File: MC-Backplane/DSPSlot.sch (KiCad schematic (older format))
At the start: 1 part

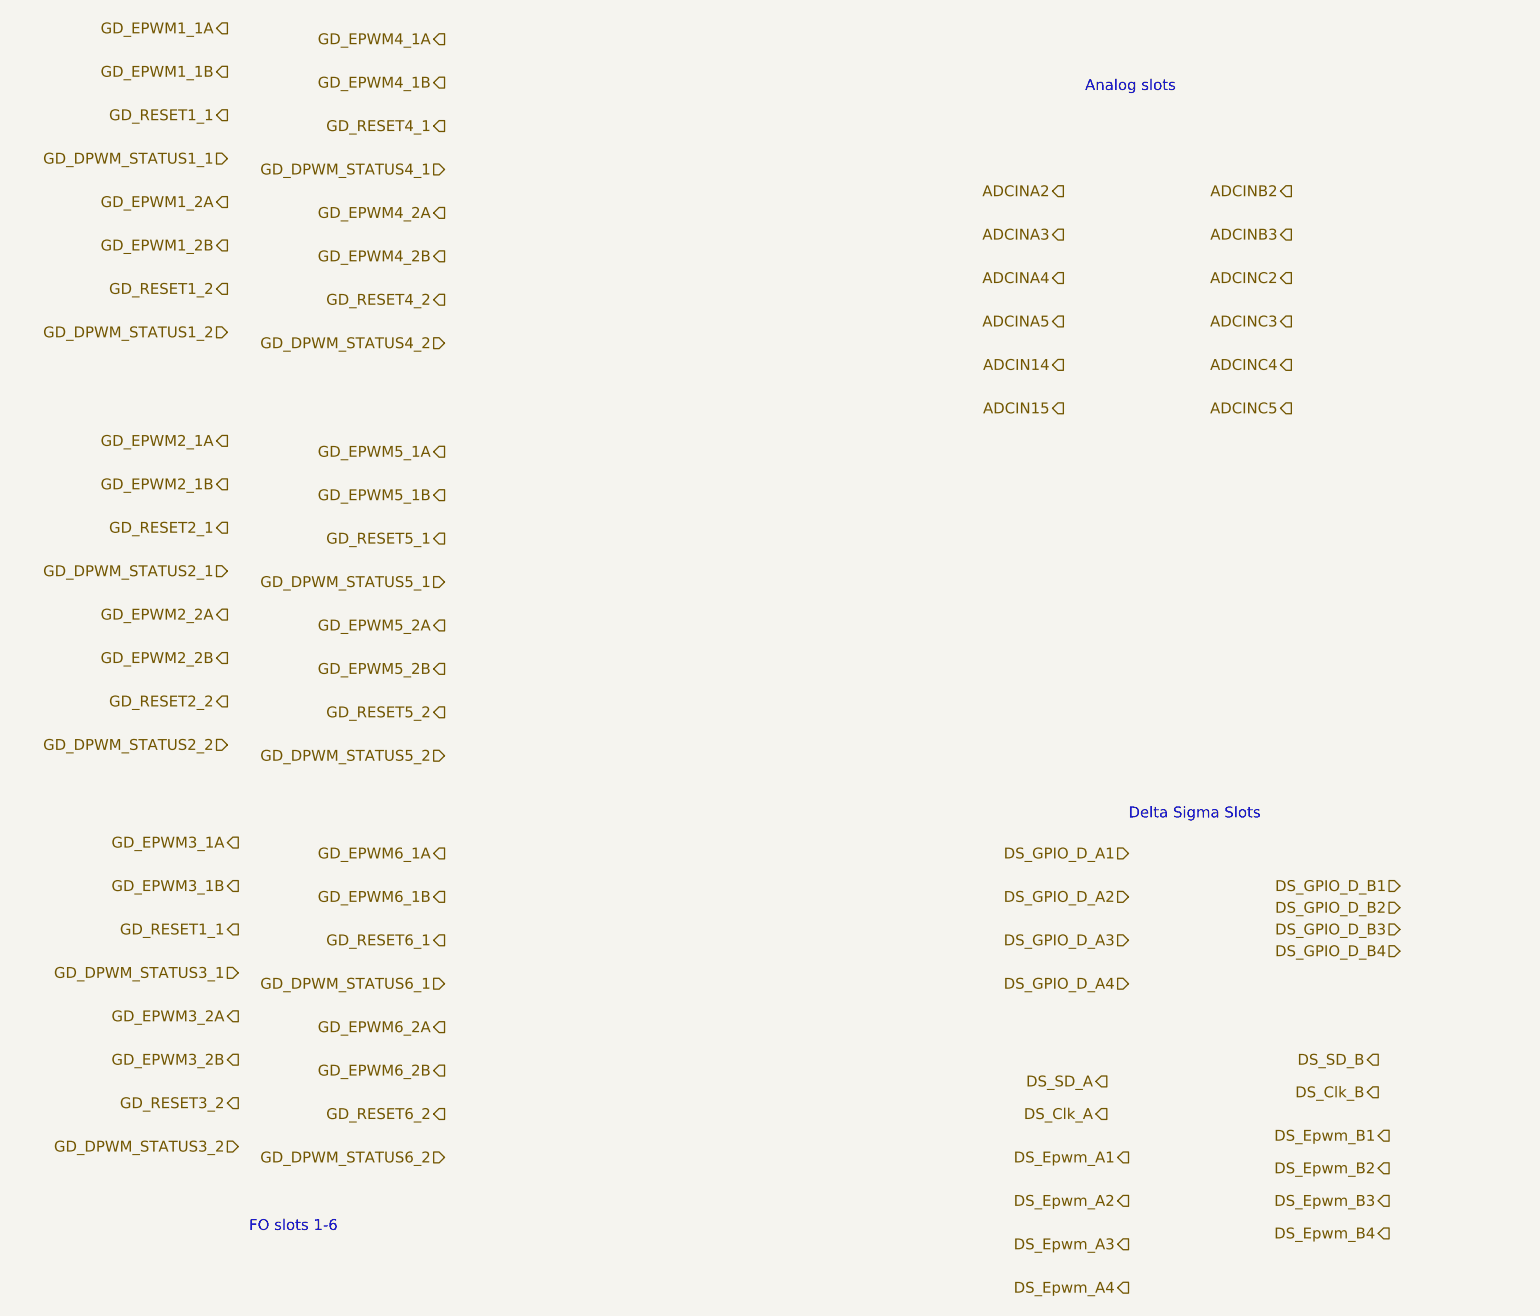
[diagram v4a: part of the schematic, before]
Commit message: Signal naming cleanup/ dsp pin pairing
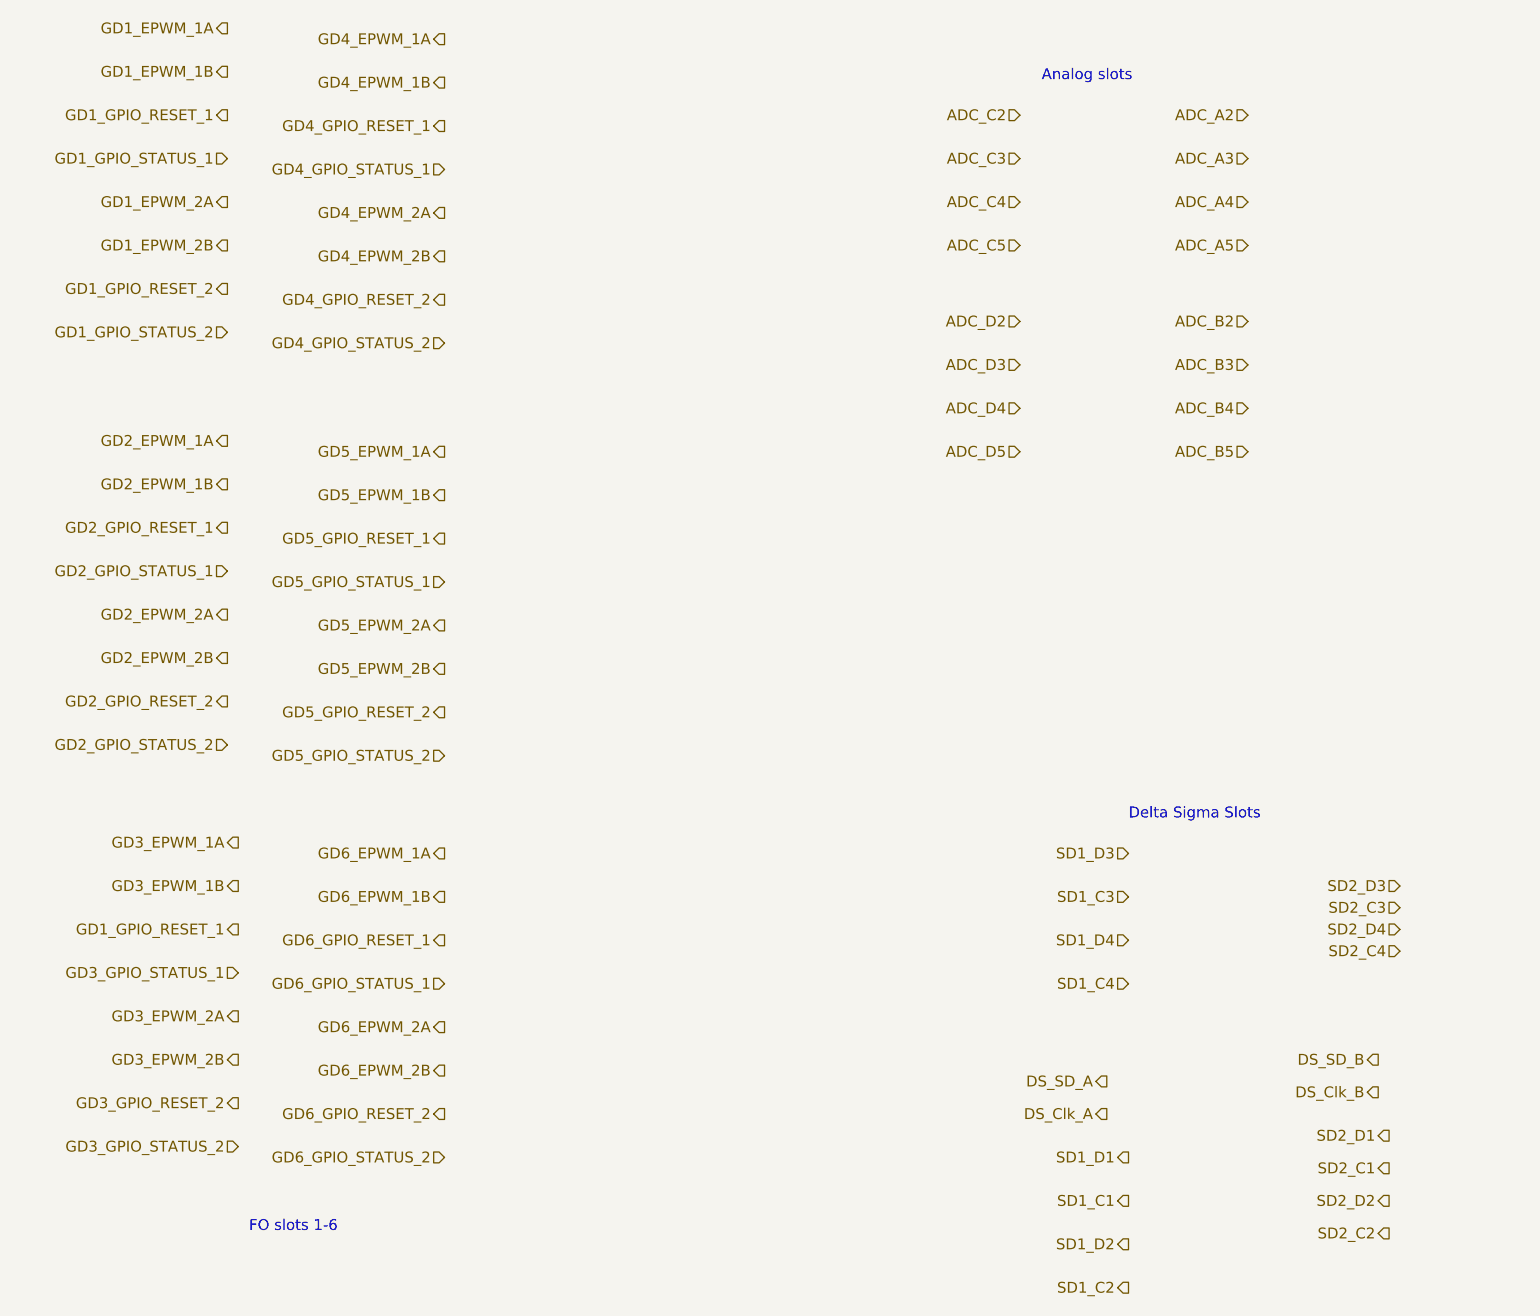
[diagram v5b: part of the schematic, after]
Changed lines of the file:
@@
 placeholder connector
 Text HLabel 1650 750  0    50   Output ~ 0
-GD_EPWM1_1A
+GD1_EPWM_1A
 Text HLabel 1650 950  0    50   Output ~ 0
-GD_EPWM1_1B
+GD1_EPWM_1B
 Text HLabel 1650 1150 0    50   Output ~ 0
-GD_RESET1_1
+GD1_GPIO_RESET_1
 Text HLabel 1650 1350 0    50   Input ~ 0
-GD_DPWM_STATUS1_1
+GD1_GPIO_STATUS_1
 Text HLabel 1650 1550 0    50   Output ~ 0
-GD_EPWM1_2A
+GD1_EPWM_2A
 Text HLabel 1650 1750 0    50   Output ~ 0
-GD_EPWM1_2B
+GD1_EPWM_2B
 Text HLabel 1650 1950 0    50   Output ~ 0
-GD_RESET1_2
+GD1_GPIO_RESET_2
 Text HLabel 1650 2150 0    50   Input ~ 0
-GD_DPWM_STATUS1_2
+GD1_GPIO_STATUS_2
 Text HLabel 1650 2650 0    50   Output ~ 0
-GD_EPWM2_1A
+GD2_EPWM_1A
 Text HLabel 1650 2850 0    50   Output ~ 0
-GD_EPWM2_1B
+GD2_EPWM_1B
 Text HLabel 1650 3050 0    50   Output ~ 0
-GD_RESET2_1
+GD2_GPIO_RESET_1
 Text HLabel 1650 3250 0    50   Input ~ 0
-GD_DPWM_STATUS2_1
+GD2_GPIO_STATUS_1
 Text HLabel 1650 3450 0    50   Output ~ 0
-GD_EPWM2_2A
+GD2_EPWM_2A
 Text HLabel 1650 3650 0    50   Output ~ 0
-GD_EPWM2_2B
+GD2_EPWM_2B
 Text HLabel 1650 3850 0    50   Output ~ 0
-GD_RESET2_2
+GD2_GPIO_RESET_2
 Text HLabel 1650 4050 0    50   Input ~ 0
-GD_DPWM_STATUS2_2
+GD2_GPIO_STATUS_2
 Text HLabel 1700 4500 0    50   Output ~ 0
-GD_EPWM3_1A
+GD3_EPWM_1A
 Text HLabel 1700 4700 0    50   Output ~ 0
-GD_EPWM3_1B
+GD3_EPWM_1B
 Text HLabel 1700 4900 0    50   Output ~ 0
-GD_RESET1_1
+GD1_GPIO_RESET_1
 Text HLabel 1700 5100 0    50   Input ~ 0
-GD_DPWM_STATUS3_1
+GD3_GPIO_STATUS_1
 Text HLabel 1700 5300 0    50   Output ~ 0
-GD_EPWM3_2A
+GD3_EPWM_2A
 Text HLabel 1700 5500 0    50   Output ~ 0
-GD_EPWM3_2B
+GD3_EPWM_2B
 Text HLabel 1700 5700 0    50   Output ~ 0
-GD_RESET3_2
+GD3_GPIO_RESET_2
 Text HLabel 1700 5900 0    50   Input ~ 0
-GD_DPWM_STATUS3_2
+GD3_GPIO_STATUS_2
 Text HLabel 2650 800  0    50   Output ~ 0
-GD_EPWM4_1A
+GD4_EPWM_1A
 Text HLabel 2650 1000 0    50   Output ~ 0
-GD_EPWM4_1B
+GD4_EPWM_1B
 Text HLabel 2650 1200 0    50   Output ~ 0
-GD_RESET4_1
+GD4_GPIO_RESET_1
 Text HLabel 2650 1400 0    50   Input ~ 0
-GD_DPWM_STATUS4_1
+GD4_GPIO_STATUS_1
 Text HLabel 2650 1600 0    50   Output ~ 0
-GD_EPWM4_2A
+GD4_EPWM_2A
 Text HLabel 2650 1800 0    50   Output ~ 0
-GD_EPWM4_2B
+GD4_EPWM_2B
 Text HLabel 2650 2000 0    50   Output ~ 0
-GD_RESET4_2
+GD4_GPIO_RESET_2
 Text HLabel 2650 2200 0    50   Input ~ 0
-GD_DPWM_STATUS4_2
+GD4_GPIO_STATUS_2
 Text HLabel 2650 4100 0    50   Input ~ 0
-GD_DPWM_STATUS5_2
+GD5_GPIO_STATUS_2
 Text HLabel 2650 3900 0    50   Output ~ 0
-GD_RESET5_2
+GD5_GPIO_RESET_2
 Text HLabel 2650 3700 0    50   Output ~ 0
-GD_EPWM5_2B
+GD5_EPWM_2B
 Text HLabel 2650 3500 0    50   Output ~ 0
-GD_EPWM5_2A
+GD5_EPWM_2A
 Text HLabel 2650 3300 0    50   Input ~ 0
-GD_DPWM_STATUS5_1
+GD5_GPIO_STATUS_1
 Text HLabel 2650 3100 0    50   Output ~ 0
-GD_RESET5_1
+GD5_GPIO_RESET_1
 Text HLabel 2650 2900 0    50   Output ~ 0
-GD_EPWM5_1B
+GD5_EPWM_1B
 Text HLabel 2650 2700 0    50   Output ~ 0
-GD_EPWM5_1A
+GD5_EPWM_1A
 Text HLabel 2650 5950 0    50   Input ~ 0
-GD_DPWM_STATUS6_2
+GD6_GPIO_STATUS_2
 Text HLabel 2650 5750 0    50   Output ~ 0
-GD_RESET6_2
+GD6_GPIO_RESET_2
 Text HLabel 2650 5550 0    50   Output ~ 0
-GD_EPWM6_2B
+GD6_EPWM_2B
 Text HLabel 2650 5350 0    50   Output ~ 0
-GD_EPWM6_2A
+GD6_EPWM_2A
 Text HLabel 2650 5150 0    50   Input ~ 0
-GD_DPWM_STATUS6_1
+GD6_GPIO_STATUS_1
 Text HLabel 2650 4950 0    50   Output ~ 0
-GD_RESET6_1
+GD6_GPIO_RESET_1
 Text HLabel 2650 4750 0    50   Output ~ 0
-GD_EPWM6_1B
+GD6_EPWM_1B
 Text HLabel 2650 4550 0    50   Output ~ 0
-GD_EPWM6_1A
+GD6_EPWM_1A
 Text Notes 1750 6300 0    50   ~ 0
 FO slots 1-6
@@
 Text HLabel 8800 1350 0    50   Input ~ 0
 24V
-Text HLabel 5500 1500 0    50   Output ~ 0
-ADCINA2
-Text HLabel 5500 1700 0    50   Output ~ 0
-ADCINA3
-Text HLabel 5500 1900 0    50   Output ~ 0
-ADCINA4
-Text HLabel 5500 2100 0    50   Output ~ 0
-ADCINA5
-Text HLabel 5500 2300 0    50   Output ~ 0
-ADCIN14
-Text HLabel 5500 2500 0    50   Output ~ 0
-ADCIN15
-Text HLabel 6550 1500 0    50   Output ~ 0
-ADCINB2
-Text HLabel 6550 1700 0    50   Output ~ 0
-ADCINB3
-Text HLabel 6550 1900 0    50   Output ~ 0
-ADCINC2
-Text HLabel 6550 2100 0    50   Output ~ 0
-ADCINC3
-Text HLabel 6550 2300 0    50   Output ~ 0
-ADCINC4
-Text HLabel 6550 2500 0    50   Output ~ 0
-ADCINC5
 Text HLabel 5800 5950 0    50   Output ~ 0
-DS_Epwm_A1
+SD1_D1
 Text HLabel 5800 6150 0    50   Output ~ 0
-DS_Epwm_A2
+SD1_C1
 Text HLabel 5800 6350 0    50   Output ~ 0
-DS_Epwm_A3
+SD1_D2
 Text HLabel 5800 6550 0    50   Output ~ 0
-DS_Epwm_A4
+SD1_C2
 Text HLabel 5700 5600 0    50   Output ~ 0
 DS_SD_A
@@
 DS_Clk_A
 Text HLabel 5800 4550 0    50   Input ~ 0
-DS_GPIO_D_A1
+SD1_D3
 Text HLabel 5800 4750 0    50   Input ~ 0
-DS_GPIO_D_A2
+SD1_C3
 Text HLabel 5800 4950 0    50   Input ~ 0
-DS_GPIO_D_A3
+SD1_D4
 Text HLabel 5800 5150 0    50   Input ~ 0
-DS_GPIO_D_A4
+SD1_C4
 Text HLabel 7000 5850 0    50   Output ~ 0
-DS_Epwm_B1
+SD2_D1
 Text HLabel 7000 6000 0    50   Output ~ 0
-DS_Epwm_B2
+SD2_C1
 Text HLabel 7000 6150 0    50   Output ~ 0
-DS_Epwm_B3
+SD2_D2
 Text HLabel 7000 6300 0    50   Output ~ 0
-DS_Epwm_B4
+SD2_C2
 Text HLabel 6950 5500 0    50   Output ~ 0
 DS_SD_B
@@
 DS_Clk_B
 Text HLabel 7050 4700 0    50   Input ~ 0
-DS_GPIO_D_B1
+SD2_D3
 Text HLabel 7050 4800 0    50   Input ~ 0
-DS_GPIO_D_B2
+SD2_C3
 Text HLabel 7050 4900 0    50   Input ~ 0
-DS_GPIO_D_B3
+SD2_D4
 Text HLabel 7050 5000 0    50   Input ~ 0
-DS_GPIO_D_B4
-Text Notes 5600 1050 0    50   ~ 0
+SD2_C4
+Text Notes 5400 1000 0    50   ~ 0
 Analog slots
 Text Notes 5800 4400 0    50   ~ 0
@@
 Text Notes 8750 900  0    50   ~ 0
 Get final connector and pinout from jacob
+Text HLabel 6350 1150 0    50   Input ~ 0
+ADC_A2
+Text HLabel 6350 1350 0    50   Input ~ 0
+ADC_A3
+Text HLabel 6350 1550 0    50   Input ~ 0
+ADC_A4
+Text HLabel 6350 1750 0    50   Input ~ 0
+ADC_A5
+Text HLabel 6350 2100 0    50   Input ~ 0
+ADC_B2
+Text HLabel 6350 2300 0    50   Input ~ 0
+ADC_B3
+Text HLabel 5300 1150 0    50   Input ~ 0
+ADC_C2
+Text HLabel 5300 1350 0    50   Input ~ 0
+ADC_C3
+Text HLabel 5300 1550 0    50   Input ~ 0
+ADC_C4
+Text HLabel 5300 1750 0    50   Input ~ 0
+ADC_C5
+Text HLabel 6350 2500 0    50   Input ~ 0
+ADC_B4
+Text HLabel 6350 2700 0    50   Input ~ 0
+ADC_B5
+Text HLabel 5300 2100 0    50   Input ~ 0
+ADC_D2
+Text HLabel 5300 2300 0    50   Input ~ 0
+ADC_D3
+Text HLabel 5300 2500 0    50   Input ~ 0
+ADC_D4
+Text HLabel 5300 2700 0    50   Input ~ 0
+ADC_D5
 $EndSCHEMATC
